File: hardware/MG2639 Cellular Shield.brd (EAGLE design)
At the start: 53.3 x 73.7 mm, 54 parts, among them J1 SIMHOLDER, J2 ARDUINO_R3_SHIELD, Q1 MMBT2222A, U1 SPX29302, U3 MG2639V3

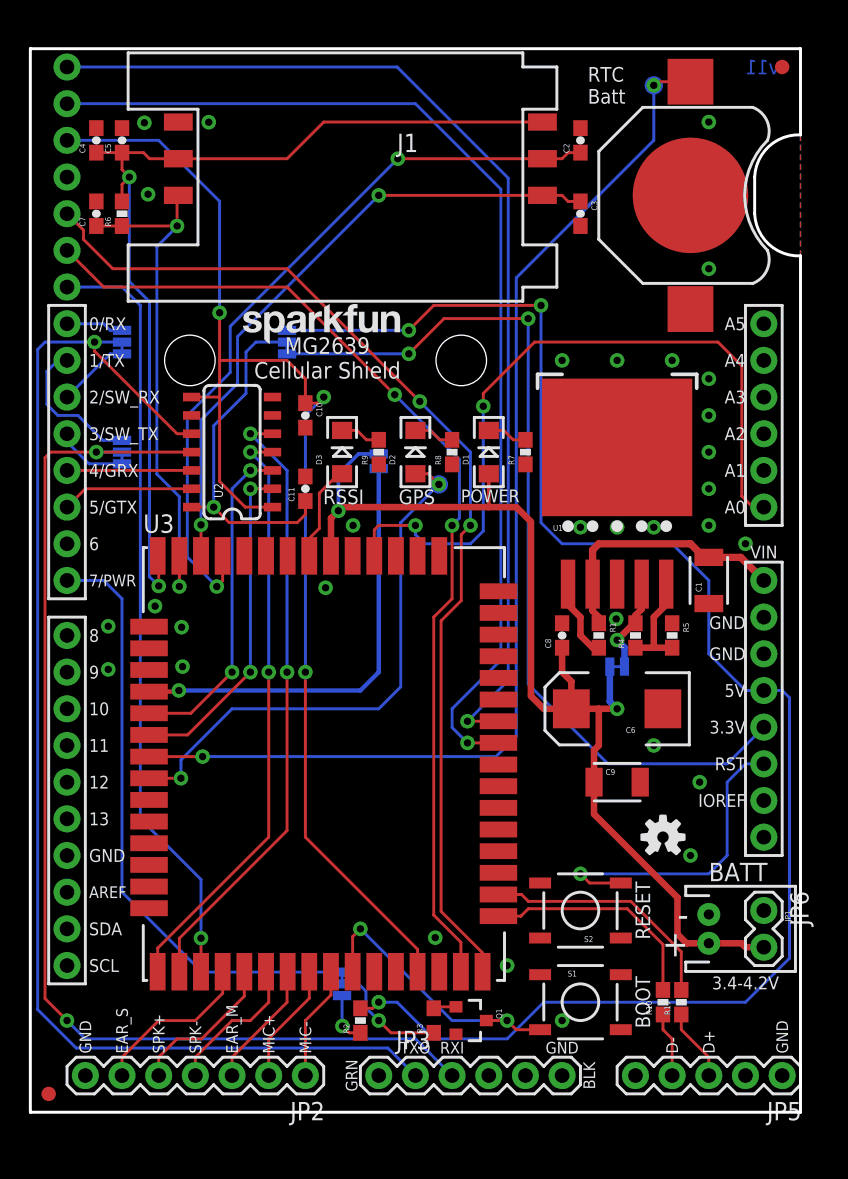
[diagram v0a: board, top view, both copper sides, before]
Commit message: Adding stand-off holes. Moving GPS UART to pins 8/9 (better support for faster buad rates). Adding jumpers to select hardware UART for GPS too.
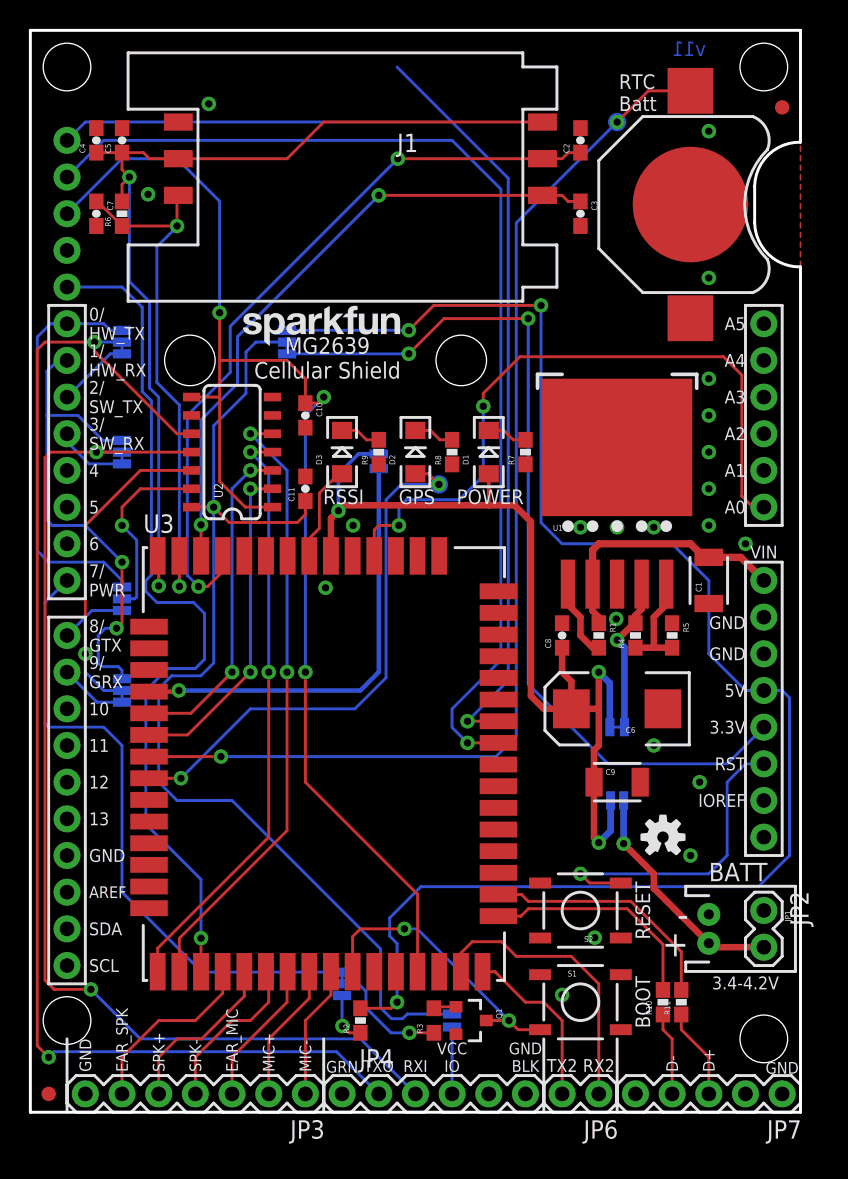
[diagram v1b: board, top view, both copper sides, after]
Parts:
- added JP7: USB, SparkFun-Connectors:1X05
- added SJ10, SJ7, SJ9: (no value), SparkFun-Passives:PAD-JUMPER-3-2OF3_NC_BY_TRACE_YES_SILK_FULL_BOX
- added SJ8: FTDI_VCCIO, SparkFun-Passives:PAD-JUMPER-2-NO_YES_SILK
- added STANDOFF1, STANDOFF2, STANDOFF3, STANDOFF4: STAND-OFF, SparkFun-Electromechanical:STAND-OFF
- JP2: value AUDIO -> M02PTH; device SparkFun-Connectors:1X07 -> SparkFun-Connectors:1X02
- JP3: value FTDI_BASICPTH -> AUDIO; device SparkFun-Connectors:FTDI_BASIC -> SparkFun-Connectors:1X07
- JP4: value (none) -> FTDI_BASICPTH; device SparkFun-Connectors:1X07 -> SparkFun-Connectors:FTDI_BASIC
- JP5: value (none) -> MISC
- JP6: value M02PTH -> UART2
- SJ1: value (none) -> BOOT; device SparkFun-Passives:PAD-JUMPER-2-NC_BY_TRACE_YES_SILK -> SparkFun-Passives:PAD-JUMPER-3-2OF3_NC_BY_TRACE_YES_SILK_FULL_BOX
- SJ2: value (none) -> VBAT1
- SJ3: value (none) -> VBAT_EN; device SparkFun-Passives:PAD-JUMPER-3-2OF3_NC_BY_TRACE_YES_SILK_FULL_BOX -> SparkFun-Passives:PAD-JUMPER-2-NO_YES_SILK
- SJ4: device SparkFun-Passives:PAD-JUMPER-3-2OF3_NC_BY_TRACE_YES_SILK_FULL_BOX -> SparkFun-Passives:PAD-JUMPER-2-NC_BY_TRACE_YES_SILK
- moved JP5 81.5 mm to (2.54, 67.3), flipped to the bottom, turned to 270 degrees
- moved JP4 73.6 mm to (21.6, 1.27), flipped to the top, turned to 0 degrees
- moved SJ1 36.3 mm to (21.6, 8.89), turned to 90 degrees
- moved JP2 33.7 mm to (50.8, 14.0), turned to 270 degrees
- moved SJ3 22.9 mm to (40.6, 21.6), turned to 180 degrees
- moved JP6 17.1 mm to (39.4, 1.27), turned to 180 degrees
- moved SJ5 13.7 mm to (17.8, 53.3)
- moved SJ4 10.4 mm to (24.1, 45.1)
- moved SJ6 7.62 mm to (6.35, 45.7)
- moved JP3 5.24 mm to (19.1, 1.27), turned to 180 degrees
- moved SJ2 4.19 mm to (40.6, 26.7)
- moved TP2 3.59 mm to (40.6, 68.6)
- moved FID2 2.79 mm to (52.1, 69.6)
- moved BAT1 0.63 mm to (45.7, 62.9)
- moved LOGO1 0.13 mm to (14.2, 52.6)
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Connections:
- new net GRX-SOFT: J2.D9, SJ10.3
- new net GTX-SOFT: J2.D8, SJ9.3
- new net N$11: JP4.VCC, SJ8.1
- new net N$12: JP1.2, JP2.2, SJ3.2
- net !SYSRST: now also JP5.5; no longer JP4.7
- net 3.3V: now also SJ5.3; no longer SJ4.3
- net 3.8V: now also SJ3.1, SJ4.1; no longer JP1.2, JP6.2, SJ1.1
- net 5V: now also SJ5.1; no longer SJ4.1
- net EAR_L: now also JP3.6; no longer JP2.6
- net GND: now also JP2.1, JP3.7, JP4.GND, JP5.4, JP7.1; no longer JP2.7, JP3.GND, JP4.4, JP5.1, JP6.1
- net GPIO1/SCL: now also JP5.1; no longer JP4.1
- net GPIO2/SDA: now also JP5.2; no longer JP4.2
- net GRX-HV: now also SJ10.2; no longer J2.D4
- net GTX-HV: now also SJ9.2; no longer J2.D5
- net MIC_N0: now also JP3.1; no longer JP2.1
- net MIC_P0: now also JP3.2; no longer JP2.2
- net MIC_P1: now also JP3.3; no longer JP2.3
- net N$10: now also JP7.3; no longer JP5.3
- net N$2: now also JP7.4; no longer JP5.4
- net N$5: now also SJ1.2; no longer SJ3.2
- net N$6: now also SJ1.1; no longer SJ3.1
- net ON/OFF: now also SJ1.3; no longer SJ3.3
- net RECN: now also JP3.4; no longer JP2.4
- net RECP: now also JP3.5; no longer JP2.5
- net RX-HV: now also JP4.TXO, SJ6.2; no longer JP3.TXO, SJ5.2
- net RX-SOFT: now also J2.D3; no longer J2.D2
- net RX2-2.8V: now also JP6.1; no longer JP4.6
- net RXI: now also SJ7.1, SJ9.1; no longer SJ6.1
- net TX-HV: now also JP4.RXI, SJ7.2; no longer JP3.RXI, SJ6.2
- net TX-SOFT: now also J2.D2, SJ7.3; no longer J2.D3, SJ5.3
- net TX2-2.8V: now also JP6.2; no longer JP4.5
- net TXO: now also SJ10.1, SJ6.1; no longer SJ5.1
- net VCCB: now also SJ5.2, SJ8.2; no longer SJ4.2
- net VDDIO: now also JP5.3; no longer JP4.3
- net V_GPS: now also SJ4.2; no longer SJ1.2
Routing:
- net TX2-2.8V: track 73.2 -> 12.0 mm, vias 2 -> 0
- net VCCB: track 24.3 -> 75.7 mm
- net RX2-2.8V: track 70.2 -> 20.0 mm, vias 2 -> 0
- net TXO: track 10.2 -> 34.9 mm, vias 0 -> 2
- net RXI: track 4.00 -> 28.4 mm
- net N$12: track 0.00 -> 16.3 mm, vias 0 -> 1
- net GRX-HV: track 8.63 -> 22.2 mm, vias 0 -> 1
- net 3.8V: track 76.0 -> 66.5 mm, vias 2 -> 3
- net !SYSRST: track 53.5 -> 59.8 mm
- net GRX-SOFT: track 0.00 -> 4.67 mm
- net N$11: track 0.00 -> 4.63 mm
- net GTX-SOFT: track 0.00 -> 4.53 mm
- net GPIO1/SCL: track 74.7 -> 79.0 mm
- net N$4: track 6.69 -> 10.9 mm
- net RING: track 51.2 -> 47.1 mm
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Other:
- board size 53.3 x 73.7 mm -> 53.3 x 74.9 mm
- board text added: "0/ HW_TX"
- board text added: "1/ HW_RX"
- board text added: "2/ SW_TX"
- board text added: "3/ SW_RX"
- board text added: "4"
- board text added: "5"
- board text added: "7/ PWR"
- board text added: "8/ GTX"
- board text added: "9/ GRX"
- board text added: "Connects FTDI VCC to VCC-IO"
- board text added: "EAR_MIC"
- board text added: "EAR_SPK"
- board text added: "GND BLK"
- board text added: "GPS_RX"
- board text added: "GPS_TX"
- board text added: "SJ2"
- board text added: "SJ3"
- board text added: "SJ4"
- board text added: "SJ8"
- board text added: "SW/8"
- board text added: "SW/9"
- board text added: "VBAT_EN"
- board text added: "VCC IO"
- board text removed: "0/RX"
- board text removed: "1/TX"
- board text removed: "2/SW_RX"
- board text removed: "3/SW_TX"
- board text removed: "4/GRX"
- board text removed: "5/GTX"
- board text removed: "7/PWR"
- board text removed: "8"
- board text removed: "9"
- board text removed: "BLK"
- board text removed: "EAR_M"
- board text removed: "EAR_S"
- board text removed: "SJ1"
- board text removed: "SJ6"

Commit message: Defaulting TXB0104 HV to 5V. Fixing connector names. Adding measures.
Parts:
- removed J1: SIMHOLDER, SparkFun-Connectors:SIMHOLDER
- removed J2: ARDUINO_R3_SHIELD, SparkFun-Boards:UNO_R3_SHIELD_NOLABELS
- added JP8: FTDI_BASICPTH, SparkFun-Connectors:FTDI_BASIC
- added JP9: USB, SparkFun-Connectors:1X05
- JP3: value AUDIO -> ARDUINO_R3_SHIELD; device SparkFun-Connectors:1X07 -> SparkFun-Boards:UNO_R3_SHIELD_NOLABELS
- JP4: value FTDI_BASICPTH -> SIMHOLDER; device SparkFun-Connectors:FTDI_BASIC -> SparkFun-Connectors:SIMHOLDER
- JP5: value MISC -> AUDIO; device SparkFun-Connectors:1X05 -> SparkFun-Connectors:1X07
- JP6: value UART2 -> MISC; device SparkFun-Connectors:1X02 -> SparkFun-Connectors:1X05
- JP7: value USB -> UART2; device SparkFun-Connectors:1X05 -> SparkFun-Connectors:1X02
- U2: value (none) -> TXB0104
- moved JP6 75.6 mm to (2.54, 67.3), flipped to the bottom, turned to 270 degrees
- moved JP5 68.1 mm to (19.1, 1.27), flipped to the top, turned to 180 degrees
- moved JP4 63.5 mm to (22.9, 64.8), turned to 180 degrees
- moved JP3 19.1 mm to (0.00, 0.00), turned to 0 degrees
- moved JP7 12.7 mm to (39.4, 1.27)
- turned SJ5 to 90 degrees
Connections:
- new net JP9: JP3.D8
- net !SYSRST: now also JP6.5; no longer JP5.5
- net 3.3V: now also JP3.3.3V, SJ5.1; no longer J2.3.3V, SJ5.3
- net 5V: now also JP3.5V, SJ5.3; no longer J2.5V, SJ5.1
- net A1: now also JP3.A1; no longer J2.A1
- net A2: now also JP3.A2; no longer J2.A2
- net A3: now also JP3.A3; no longer J2.A3
- net A4: now also JP3.A4; no longer J2.A4
- net A5: now also JP3.A5; no longer J2.A5
- net CELL_RESET: now also JP3.D6; no longer J2.D6
- net EAR_L: now also JP5.6; no longer JP3.6
- net GND: now also JP3.GND@0, JP3.GND@1, JP3.GND@2, JP4.C5, JP5.7, JP6.4, JP8.GND, JP9.1; no longer J1.C5, J2.GND@0, J2.GND@1, J2.GND@2, JP3.7, JP4.GND, JP5.4, JP7.1
- net GPIO1/SCL: now also JP6.1; no longer JP5.1
- net GPIO2/SDA: now also JP6.2; no longer JP5.2
- net GRX-SOFT: now also JP3.D9; no longer J2.D9
- net GTX-SOFT: no longer J2.D8
- net MIC_N0: now also JP5.1; no longer JP3.1
- net MIC_P0: now also JP5.2; no longer JP3.2
- net MIC_P1: now also JP5.3; no longer JP3.3
- net N$10: now also JP9.3; no longer JP7.3
- net N$11: now also JP8.VCC; no longer JP4.VCC
- net N$2: now also JP9.4; no longer JP7.4
- net ON/OFF: now also JP3.D7; no longer J2.D7
- net RECN: now also JP5.4; no longer JP3.4
- net RECP: now also JP5.5; no longer JP3.5
- net RESET: now also JP3.RES; no longer J2.RES
- net RING: now also JP3.A0; no longer J2.A0
- net RX-HV: now also JP8.TXO; no longer JP4.TXO
- net RX-SOFT: now also JP3.D3; no longer J2.D3
- net RX2-2.8V: now also JP7.1; no longer JP6.1
- net RXI: now also JP3.RX; no longer J2.RX
- net SIM_CLK: now also JP4.C3; no longer J1.C3
- net SIM_DATA: now also JP4.C7; no longer J1.C7
- net SIM_RST: now also JP4.C2; no longer J1.C2
- net TX-HV: now also JP8.RXI; no longer JP4.RXI
- net TX-SOFT: now also JP3.D2; no longer J2.D2
- net TX2-2.8V: now also JP7.2; no longer JP6.2
- net TXO: now also JP3.TX; no longer J2.TX
- net VDDIO: now also JP6.3; no longer JP5.3
- net VRAW: now also JP3.VIN; no longer J2.VIN
- net VSIM: now also JP4.C1, JP4.C6; no longer J1.C1, J1.C6
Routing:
- net GTX-SOFT: track 4.53 -> 2.08 mm
